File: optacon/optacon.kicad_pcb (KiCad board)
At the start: 2 copper layers, 40.6 x 78.5 mm, 20 parts, among them J1 Conn_01x12, U1 HV528, U2 HV528, U3 DRV2665

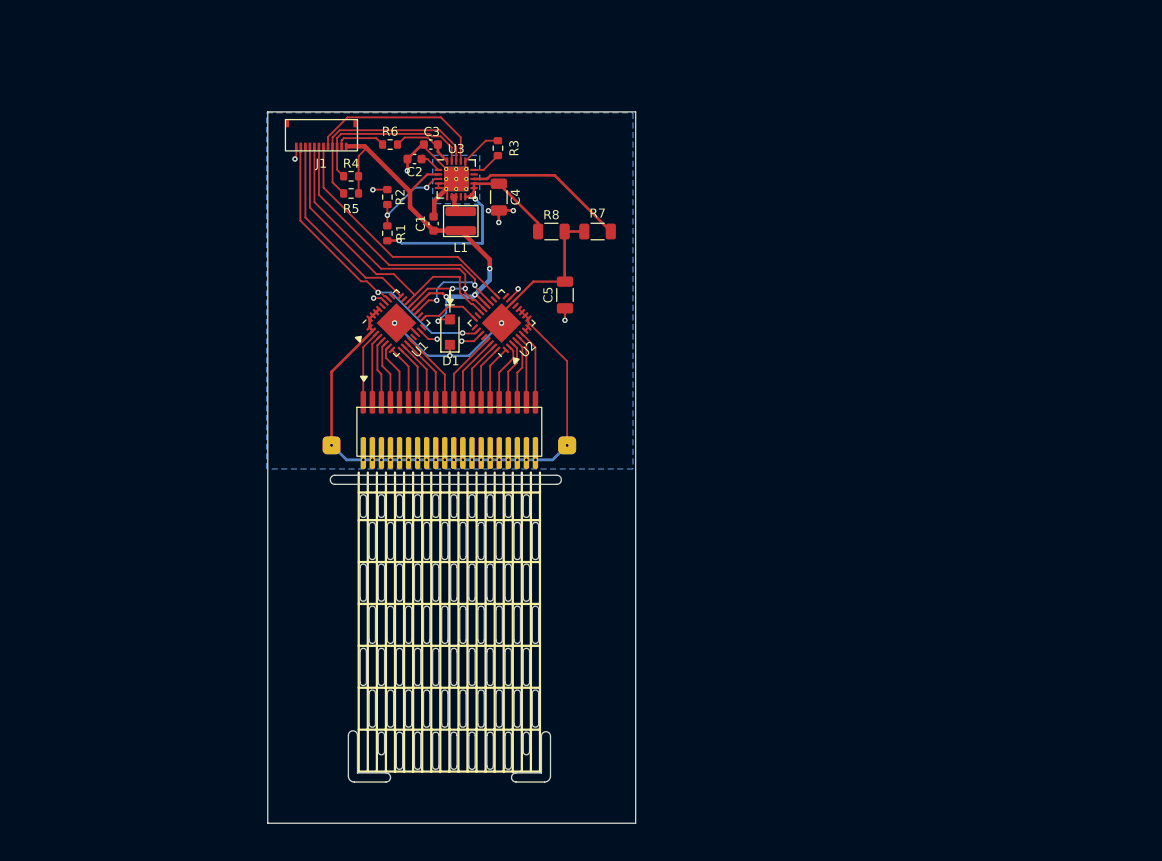
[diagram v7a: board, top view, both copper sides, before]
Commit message: WIP -added clearance for reeds center conductor header pins -removed jumper resistor & output cap on VBST -changed C4 high voltage cap to 0805, lower height above board -added C5 10µF cap at inductor -changed hole pattern on piezo to PTH for smaller holes -added copper fill under piezo for equal height -removed alignment holes around piezo, replaced with front silkscreen alignment arrows -reworked layout on DRV2665 a bit according to datasheet guidelines -moved fpc connector to top
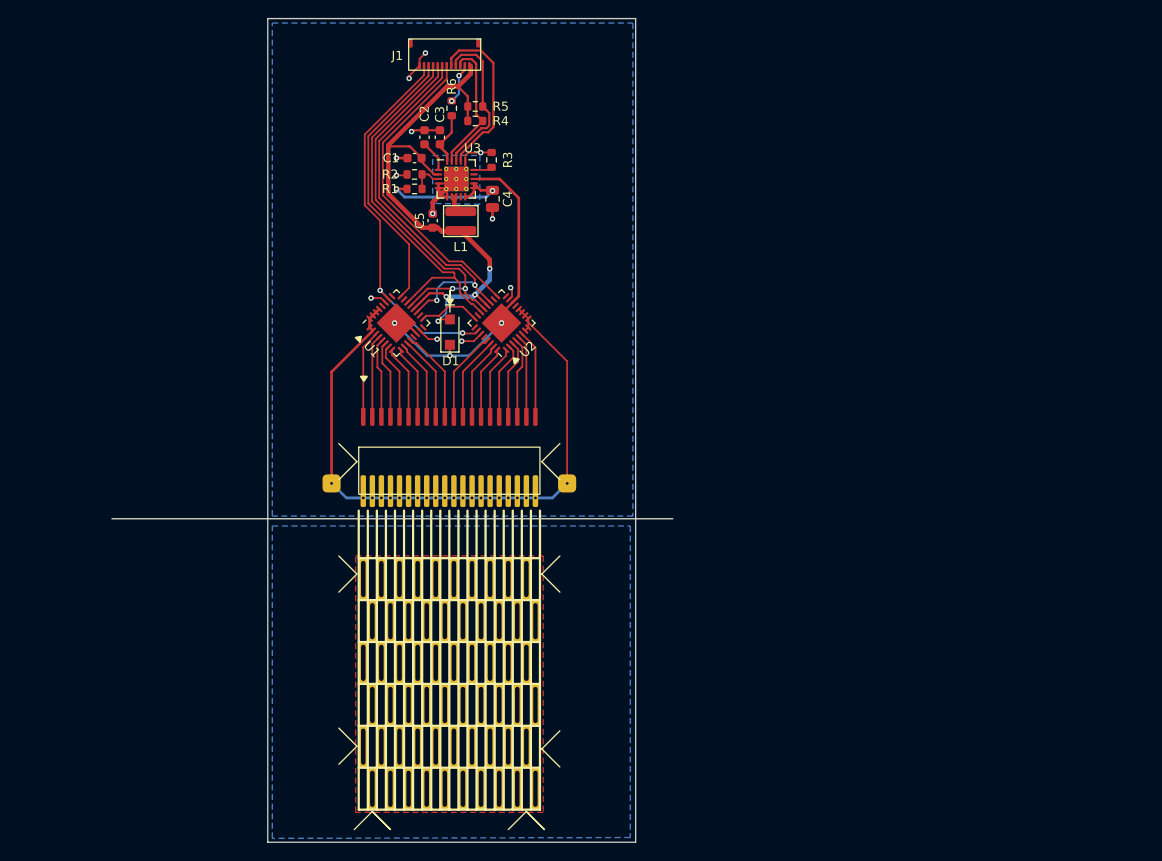
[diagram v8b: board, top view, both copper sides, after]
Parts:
- removed R7: 0R, Resistor_SMD:R_1206_3216Metric
- removed R8: DNP, Resistor_SMD:R_1206_3216Metric
- C4: footprint Capacitor_SMD:C_1206_3216Metric -> Capacitor_SMD:C_0805_2012Metric
- C5: value 0.1µF -> 10 µF; footprint Capacitor_SMD:C_1206_3216Metric -> Capacitor_SMD:C_0603_1608Metric
- R6: value 0 -> DNP
- moved C5 16.7 mm to (102.3, 62.7)
- moved R5 16.7 mm to (107.0, 50.1), turned to 180 degrees
- moved J1 16.3 mm to (103.6, 44.5)
- moved R4 15.0 mm to (107.0, 51.7), turned to 0 degrees
- moved R6 7.89 mm to (104.4, 50.3), turned to -90 degrees
- moved C1 7.52 mm to (100.3, 55.8), turned to 180 degrees
- moved R1 5.75 mm to (100.3, 59.2), turned to 0 degrees
- moved piezo1 4.20 mm to (104.0, 87.7)
- moved R2 3.91 mm to (100.3, 57.6), turned to 0 degrees
- moved C2 2.64 mm to (101.4, 53.5), turned to 90 degrees
- moved R3 1.48 mm to (108.8, 56.0)
- moved C3 1.28 mm to (103.1, 53.5), turned to 90 degrees
- moved C4 0.73 mm to (108.9, 60.3)
- turned L1 to -90 degrees
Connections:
- net /VBST renamed /hv_driver/VBST
- C5 pad 1: GND -> /VDD
- C5 pad 2: /VPP -> GND
- L1 pad 1: /VDD -> Net-(L1-Pad1)
- L1 pad 2: Net-(L1-Pad2) -> /VDD
- U3 pad 13: /VOUT -> /VPP
- U3 pad 7: Net-(L1-Pad2) -> Net-(L1-Pad1)
- U3 pad 8: Net-(L1-Pad2) -> Net-(L1-Pad1)
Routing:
- net /VOUT: track 17.8 -> 0.00 mm
- net /VDD: track 49.9 -> 62.9 mm
- net /hv_driver/VBST: track 28.5 -> 16.9 mm
- net /DOUT: track 22.0 -> 30.4 mm
- net /VBIAS: track 34.6 -> 42.5 mm
- net /LE: track 34.3 -> 42.1 mm
- net /PZT_Common: track 63.1 -> 70.4 mm
- net Net-(R1-Pad2): track 9.70 -> 3.62 mm, vias 2 -> 0
- net /DIN: track 28.7 -> 34.4 mm
- net /SCL: track 23.0 -> 17.3 mm
- net /CLK: track 38.4 -> 43.7 mm
- net /POL: track 37.8 -> 42.7 mm
- net GND: track 37.4 -> 32.8 mm, vias 11 -> 12
- net /SDA: track 19.5 -> 15.0 mm
- net /VPP: track 36.2 -> 38.9 mm
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- added copper zone on B.Cu, net /fill
- added copper zone on F.Cu, net /fill
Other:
- board size 40.6 x 78.5 mm -> 61.9 x 90.9 mm
- board text added: "v-cut"
- board text removed: "vscore"
